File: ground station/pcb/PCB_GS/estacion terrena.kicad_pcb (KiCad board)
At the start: 2 copper layers, 94 x 93.8 mm, 20 parts, among them J1 Micro-usb_lora, J2 Parte izquierda lora, J3 parte derecha lora, J4 Breakouy_micro_usb, SW1 SWITCH

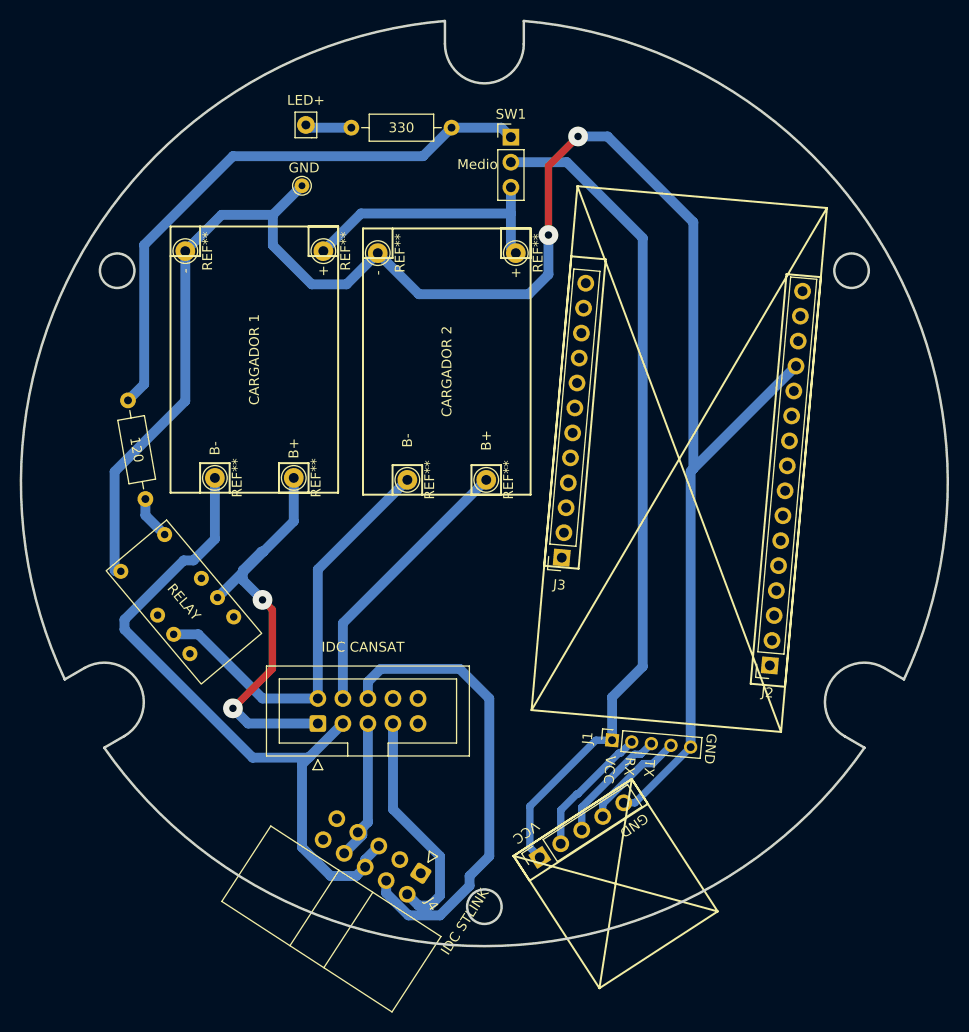
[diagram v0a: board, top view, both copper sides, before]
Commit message: Adición de modificaciones y nuevo diseño de placa
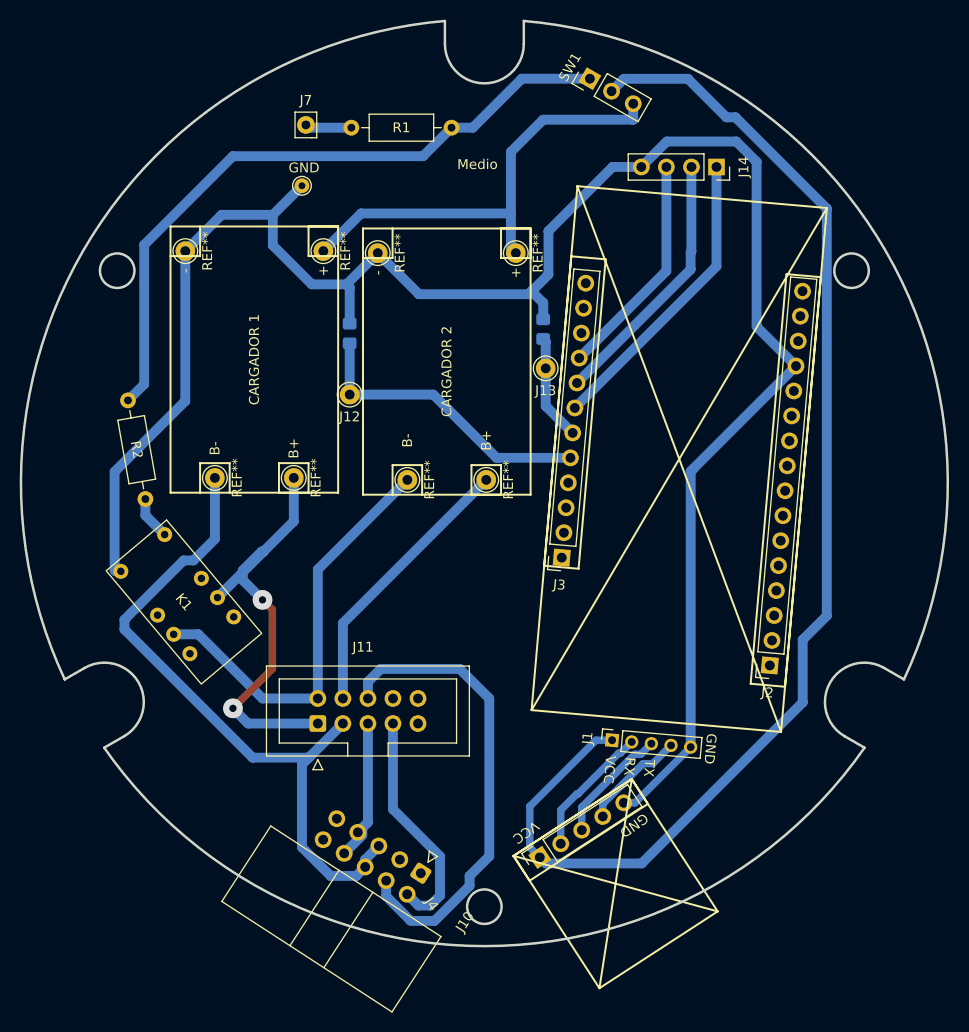
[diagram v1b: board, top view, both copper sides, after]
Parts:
- added J12: LED_CARGA_1, Connector_Pin:Pin_D1.0mm_L10.0mm, F.Cu at (135.8, 90.2)
- added J13: LED_CARGA_2, Connector_Pin:Pin_D1.0mm_L10.0mm, F.Cu at (155.7, 87.5)
- added J14: conector RGB, Connector_PinSocket_2.54mm:PinSocket_1x04_P2.54mm_Vertical, F.Cu at (173.0, 67.1)
- added R3: 10K, Resistor_SMD:R_0805_2012Metric_Pad1.20x1.40mm_HandSolder, B.Cu at (135.8, 84.0)
- added R4: 10K, Resistor_SMD:R_0805_2012Metric_Pad1.20x1.40mm_HandSolder, B.Cu at (155.5, 83.5)
- J10: renamed from IDC STLINK
- J11: renamed from IDC CANSAT
- moved SW1 9.97 mm to (160.2, 58.1), turned to 60 degrees
- renumbered LED+ to J7, RELAY to K1, 330 to R1, 120 to R2
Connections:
- J3 pad 5: unconnected-(J3-Pad5) -> /LED_CARGA_1
- J3 pad 6: unconnected-(J3-Pad6) -> /LED_CARGA_2
- J3 pad 7: unconnected-(J3-Pad7) -> /R
- J3 pad 8: unconnected-(J3-Pad8) -> /G
- J3 pad 9: unconnected-(J3-Pad9) -> /B
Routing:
- net VCC: track 85.5 -> 129.3 mm
- net /R: track 0.00 -> 30.4 mm
- net /LED_CARGA_1: track 0.00 -> 30.3 mm
- net /G: track 0.00 -> 26.7 mm
- net /B: track 0.00 -> 23.0 mm
- net /VCC_SW: track 27.5 -> 46.5 mm
- net /LED_CARGA_2: track 0.00 -> 10.8 mm
- net Net-(R1-Pad2): track 59.0 -> 68.6 mm
- net GND: track 194.9 -> 198.6 mm, vias 2 -> 0
- net /SDIO_STL: track 47.5 -> 48.1 mm

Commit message: Actualizaciones
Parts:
- added R5: 10K, Resistor_SMD:R_0805_2012Metric_Pad1.20x1.40mm_HandSolder, B.Cu at (159.9, 70.3)
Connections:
- J14 pad 4: GND -> VCC
- J3 pad 11: unconnected-(J3-Pad11) -> /VCC_SW
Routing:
- net /VCC_SW: track 46.5 -> 73.8 mm, vias 0 -> 2
- net VCC: track 129.3 -> 144.7 mm, vias 0 -> 2
- net GND: track 198.6 -> 201.3 mm
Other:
- board text added: "A"
- board text added: "B"
- board text added: "G"
- board text added: "R"

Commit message: Actualizacion
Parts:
- removed J7: POSITIVO_LED TESTIGO, Connector_Pin:Pin_D0.9mm_L10.0mm_W2.4mm_FlatFork
- removed R1: 330, Resistor_THT:R_Axial_DIN0207_L6.3mm_D2.5mm_P10.16mm_Horizontal
- moved R5 1.19 mm to (158.8, 70.1)
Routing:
- net /LED: track 4.73 -> 0.00 mm
- net /VBAT1: track 44.4 -> 41.4 mm
- net /GNDBAT2: track 43.2 -> 40.8 mm
- net VCC: track 144.7 -> 143.2 mm
- net /VCC_SW: track 73.8 -> 74.5 mm
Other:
- board text added: "ESTACION TERRENA V1 G.V.I.E"
